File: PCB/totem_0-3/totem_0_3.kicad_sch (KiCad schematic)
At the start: 97 parts, among them J1 MJ-4PP-9, J2 MJ-4PP-9, J3 Conn_01x03_Socket, J4 Conn_01x03_Socket, J5 Conn_01x12_Socket, J6 Conn_01x12_Socket, U1 xiao-ble, U2 xiao-ble, U3 74HC595, U4 74HC595

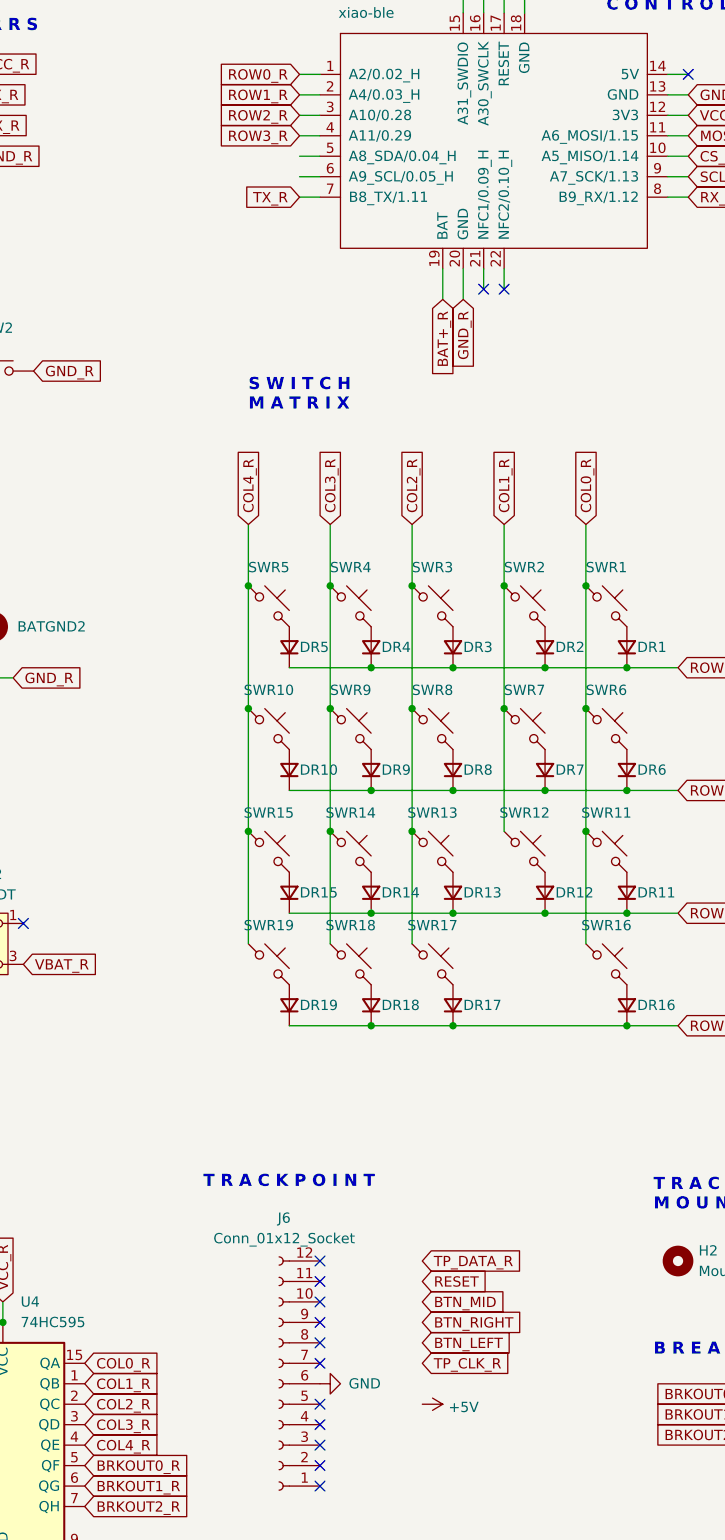
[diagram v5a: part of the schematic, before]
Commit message: sch: wire up trackpoint
Signed-off-by: Anant Thazhemadam <anant.thazhemadam@gmail.com>
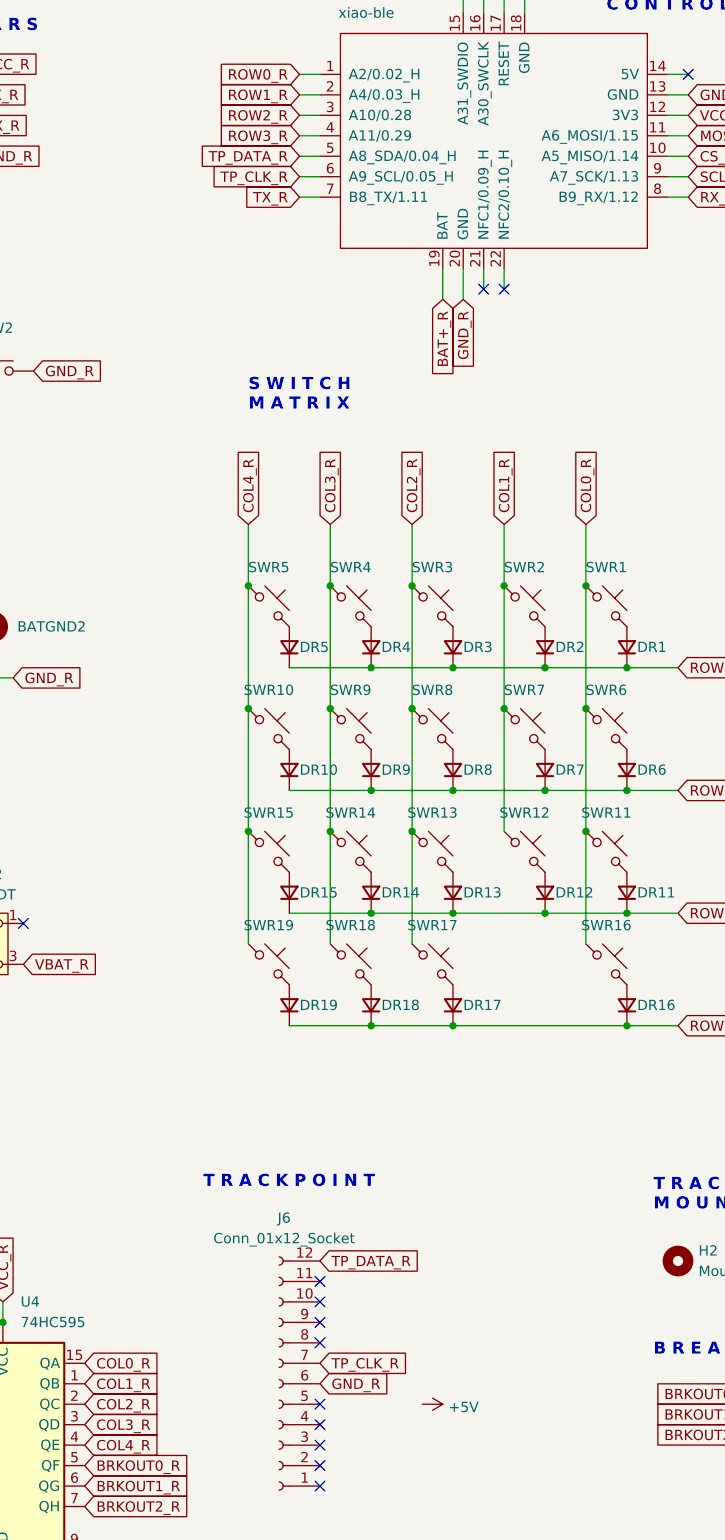
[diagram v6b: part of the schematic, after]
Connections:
- net GND is gone; now on net GND_R: J6.6 (Pin_6)
- net TP_CLK_R: now also J6.7 (Pin_7), U2.6 (A9_SCL/0.05_H)
- net TP_DATA_R: now also J6.12 (Pin_12), U2.5 (A8_SDA/0.04_H)
- no-connect marks 55 -> 53
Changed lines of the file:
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@@
 	)
 	(no_connect
-		(at 257.81 201.93)
-	)
-	(no_connect
 		(at 21.59 207.01)
 	)
@@
 	)
 	(no_connect
-		(at 257.81 189.23)
-	)
-	(no_connect
 		(at 78.74 201.93)
 	)
@@
 		)
 	)
-	(global_label "RESET"
-		(shape input)
-		(at 270.51 191.77 0)
-		(fields_autoplaced yes)
-		(effects
-			(font
-				(size 1.27 1.27)
-			)
-			(justify left)
-		)
-		(property "Intersheetrefs" "${INTERSHEET_REFS}"
-			(at 278.5067 191.77 0)
-			(effects
-				(font
-					(size 1.27 1.27)
-				)
-				(justify left)
-				(hide yes)
-			)
-		)
-	)
 	(global_label "RX_L"
 		(shape input)
@@
 		)
 	)
+	(global_label "TP_DATA_R"
+		(shape input)
+		(at 255.27 52.07 180)
+		(fields_autoplaced yes)
+		(effects
+			(font
+				(size 1.27 1.27)
+			)
+			(justify right)
+		)
+		(property "Intersheetrefs" "${INTERSHEET_REFS}"
+			(at 242.4272 52.07 0)
+			(effects
+				(font
+					(size 1.27 1.27)
+				)
+				(justify right)
+				(hide yes)
+			)
+		)
+	)
 	(global_label "VCC_L"
 		(shape input)
@@
 		)
 	)
-	(global_label "TP_DATA_R"
+	(global_label "GND_R"
 		(shape input)
-		(at 270.51 189.23 0)
+		(at 257.81 204.47 0)
 		(fields_autoplaced yes)
 		(effects
@@
 		)
 		(property "Intersheetrefs" "${INTERSHEET_REFS}"
-			(at 283.3528 189.23 0)
+			(at 266.9033 204.47 0)
 			(effects
 				(font
@@
 		)
 	)
-	(global_label "BTN_RIGHT"
-		(shape input)
-		(at 270.51 196.85 0)
-		(fields_autoplaced yes)
-		(effects
-			(font
-				(size 1.27 1.27)
-			)
-			(justify left)
-		)
-		(property "Intersheetrefs" "${INTERSHEET_REFS}"
-			(at 282.7402 196.85 0)
-			(effects
-				(font
-					(size 1.27 1.27)
-				)
-				(justify left)
-				(hide yes)
-			)
-		)
-	)
 	(global_label "COL3_R"
 		(shape input)
@@
 		)
 	)
+	(global_label "TP_DATA_R"
+		(shape input)
+		(at 257.81 189.23 0)
+		(fields_autoplaced yes)
+		(effects
+			(font
+				(size 1.27 1.27)
+			)
+			(justify left)
+		)
+		(property "Intersheetrefs" "${INTERSHEET_REFS}"
+			(at 270.6528 189.23 0)
+			(effects
+				(font
+					(size 1.27 1.27)
+				)
+				(justify left)
+				(hide yes)
+			)
+		)
+	)
 	(global_label "GND_R"
 		(shape input)
@@
 		)
 	)
-	(global_label "BTN_LEFT"
-		(shape input)
-		(at 270.51 199.39 0)
-		(fields_autoplaced yes)
-		(effects
-			(font
-				(size 1.27 1.27)
-			)
-			(justify left)
-		)
-		(property "Intersheetrefs" "${INTERSHEET_REFS}"
-			(at 281.5306 199.39 0)
-			(effects
-				(font
-					(size 1.27 1.27)
-				)
-				(justify left)
-				(hide yes)
-			)
-		)
-	)
 	(global_label "VBAT_L"
 		(shape input)
@@
 		)
 	)
-	(global_label "TP_CLK_R"
-		(shape input)
-		(at 270.51 201.93 0)
-		(fields_autoplaced yes)
-		(effects
-			(font
-				(size 1.27 1.27)
-			)
-			(justify left)
-		)
-		(property "Intersheetrefs" "${INTERSHEET_REFS}"
-			(at 282.5061 201.93 0)
-			(effects
-				(font
-					(size 1.27 1.27)
-				)
-				(justify left)
-				(hide yes)
-			)
-		)
-	)
 	(global_label "VCC_R"
 		(shape input)
@@
 		)
 	)
+	(global_label "TP_CLK_R"
+		(shape input)
+		(at 257.81 201.93 0)
+		(fields_autoplaced yes)
+		(effects
+			(font
+				(size 1.27 1.27)
+			)
+			(justify left)
+		)
+		(property "Intersheetrefs" "${INTERSHEET_REFS}"
+			(at 269.8061 201.93 0)
+			(effects
+				(font
+					(size 1.27 1.27)
+				)
+				(justify left)
+				(hide yes)
+			)
+		)
+	)
 	(global_label "ROW2_R"
 		(shape input)
@@
 		)
 	)
-	(global_label "BTN_MID"
+	(global_label "TP_CLK_R"
 		(shape input)
-		(at 270.51 194.31 0)
+		(at 255.27 54.61 180)
 		(fields_autoplaced yes)
 		(effects
@@
 				(size 1.27 1.27)
 			)
-			(justify left)
+			(justify right)
 		)
 		(property "Intersheetrefs" "${INTERSHEET_REFS}"
-			(at 280.6235 194.31 0)
+			(at 243.2739 54.61 0)
 			(effects
 				(font
 					(size 1.27 1.27)
 				)
-				(justify left)
+				(justify right)
 				(hide yes)
 			)
@@
 					(unit 1)
 				)
-			)
-		)
-	)
-	(symbol
-		(lib_id "power:GND")
-		(at 257.81 204.47 90)
-		(unit 1)
-		(exclude_from_sim no)
-		(in_bom yes)
-		(on_board yes)
-		(dnp no)
-		(fields_autoplaced yes)
-		(property "Reference" "#PWR01"
-			(at 264.16 204.47 0)
-			(effects
-				(font
-					(size 1.27 1.27)
-				)
-				(hide yes)
-			)
-		)
-		(property "Value" "GND"
-			(at 261.366 204.47 90)
-			(effects
-				(font
-					(size 1.27 1.27)
-				)
-				(justify right)
-			)
-		)
-		(property "Footprint" ""
-			(at 257.81 204.47 0)
-			(effects
-				(font
-					(size 1.27 1.27)
-				)
-				(hide yes)
-			)
-		)
-		(property "Datasheet" ""
-			(at 257.81 204.47 0)
-			(effects
-				(font
-					(size 1.27 1.27)
-				)
-				(hide yes)
-			)
-		)
-		(property "Description" "Power symbol creates a global label with name \"GND\" , ground"
-			(at 257.81 204.47 0)
-			(effects
-				(font
-					(size 1.27 1.27)
-				)
-				(hide yes)
-			)
-		)
-		(pin "1"
-		)
-		(instances
-			(project "totem_0_3"
-				(path "/4d1e609f-5432-4afb-8ee7-7d2d9aaaee48"
-					(reference "#PWR01")
-					(unit 1)
-				)

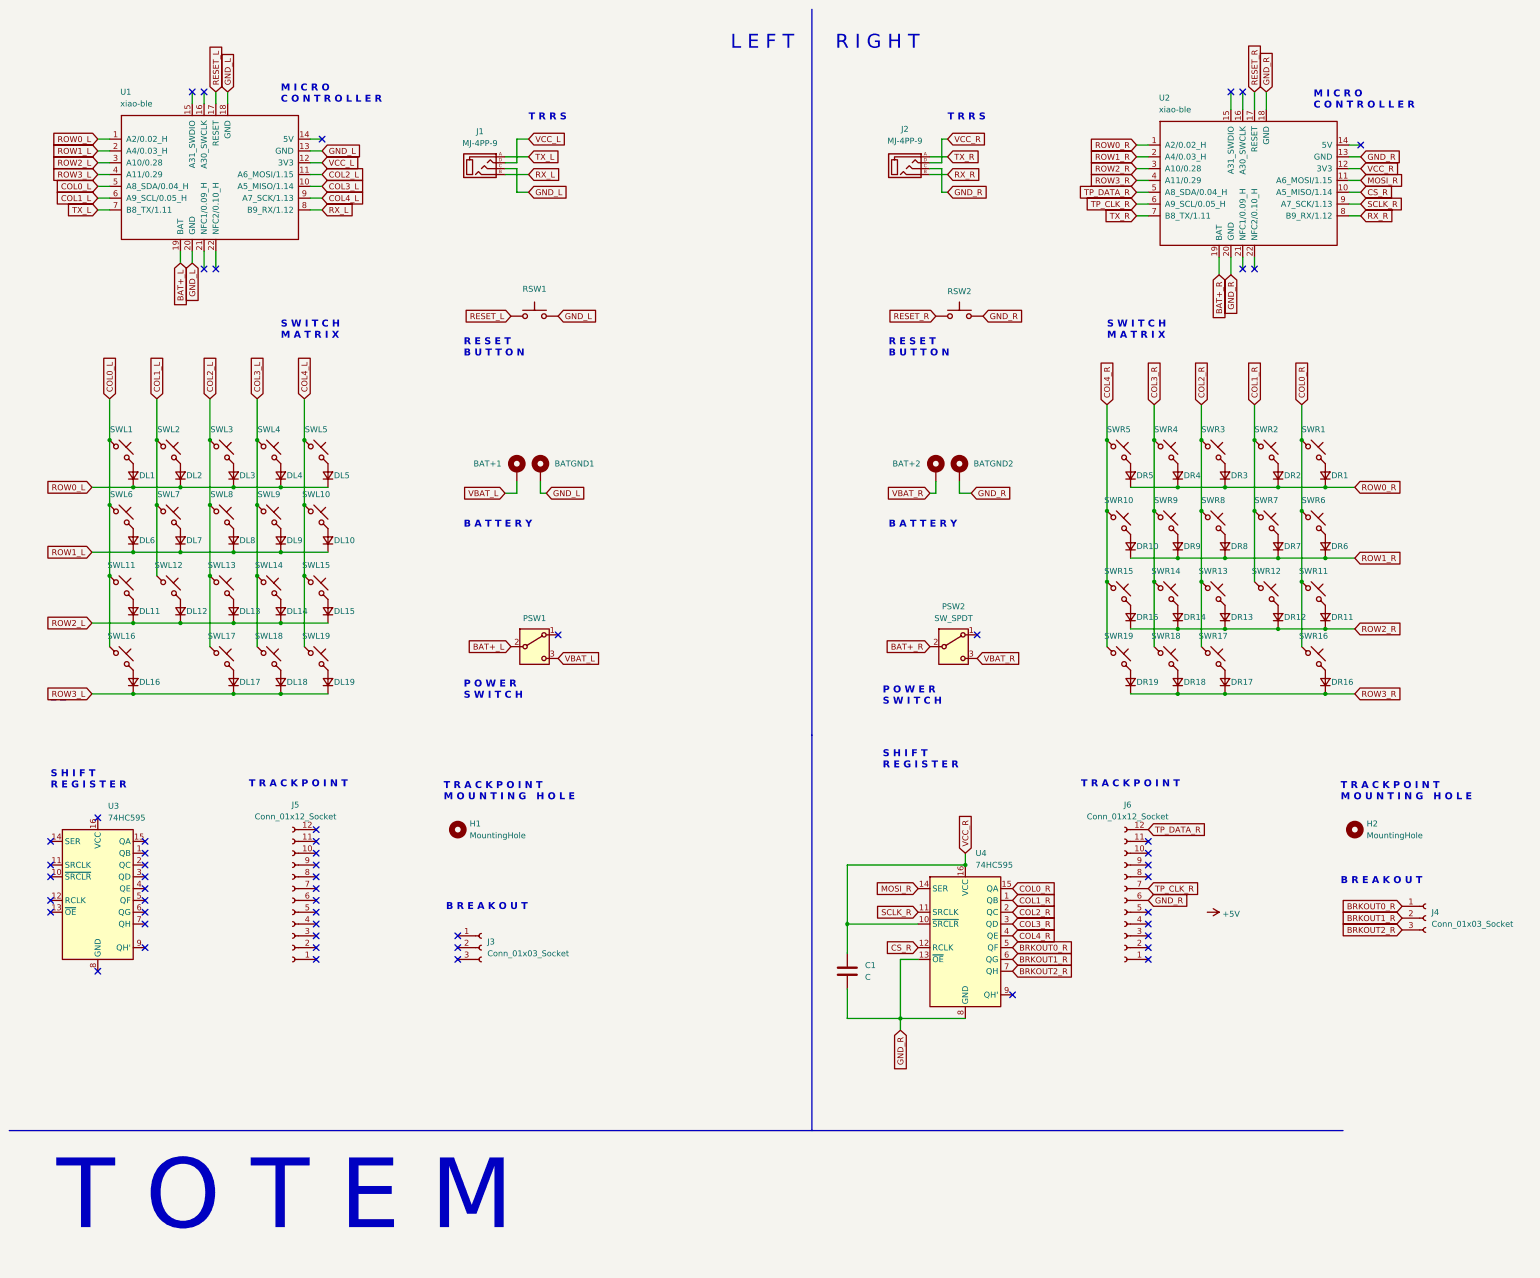
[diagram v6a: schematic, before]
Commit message: pcb: remove lhs trackpoint
Signed-off-by: Anant Thazhemadam <anant.thazhemadam@gmail.com>
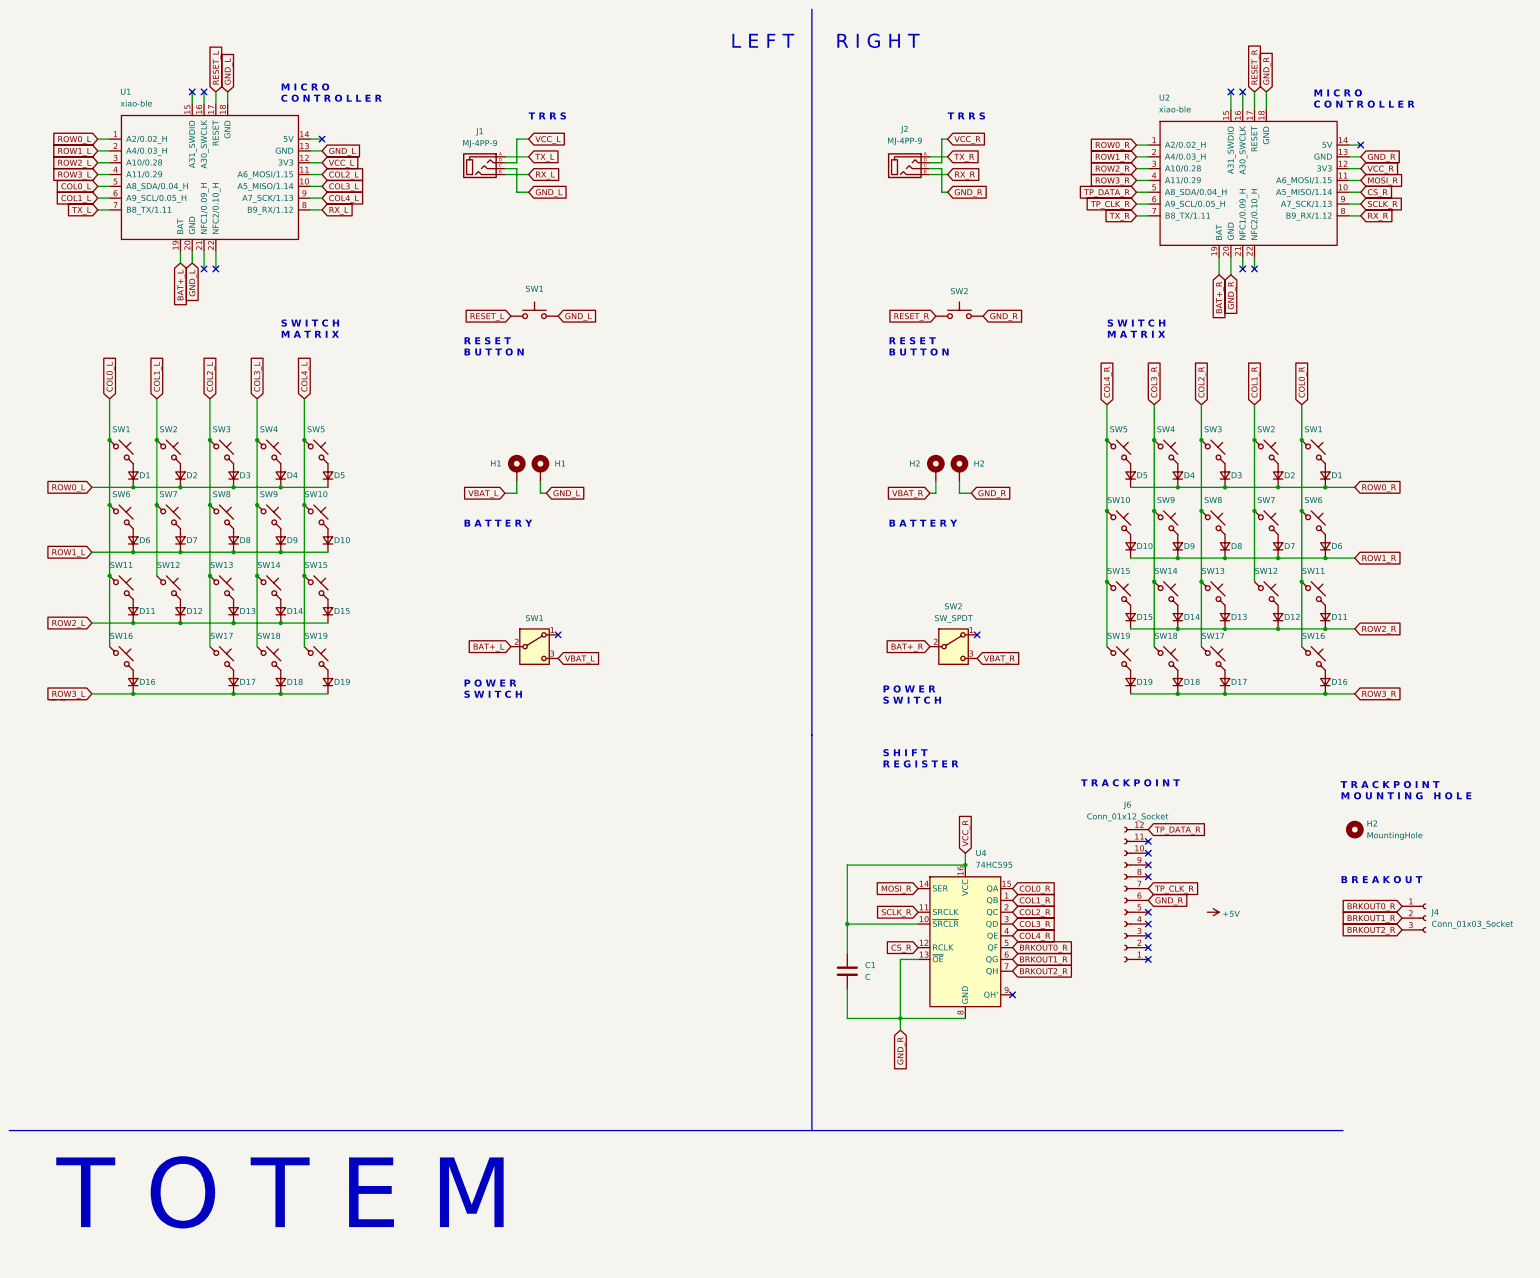
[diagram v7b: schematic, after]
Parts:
- removed H1: MountingHole, TOTEMlib:TPSensorModule, symbol Mechanical:MountingHole
- removed J3: Conn_01x03_Socket, Connector_PinHeader_2.54mm:PinHeader_1x03_P2.54mm_Vertical, symbol Connector:Conn_01x03_Socket
- removed J5: Conn_01x12_Socket, Connector_FFC-FPC:TE_1-84953-2_1x12-1MP_P1.0mm_Horizontal, symbol Connector:Conn_01x12_Socket
- removed U3: 74HC595, Package_SO:SOIC-16_3.9x9.9mm_P1.27mm, symbol 74xx:74HC595
- renumbered DL1 to D1, DR1 to D1, DL10 to D10, DR10 to D10, DR11 to D11, DL11 to D11, DR12 to D12, DL12 to D12, DR13 to D13, DL13 to D13, DR14 to D14, DL14 to D14, DR15 to D15, DL15 to D15, DR16 to D16, DL16 to D16, DR17 to D17, DL17 to D17, DL18 to D18, DR18 to D18, DL19 to D19, DR19 to D19, DL2 to D2, DR2 to D2, DL3 to D3, DR3 to D3, DR4 to D4, DL4 to D4, DR5 to D5, DL5 to D5, DR6 to D6, DL6 to D6, DL7 to D7, DR7 to D7, DL8 to D8, DR8 to D8, DR9 to D9, DL9 to D9, BAT+1 to H1, BATGND1 to H1, BATGND2 to H2, BAT+2 to H2, PSW1 to SW1, RSW1 to SW1, SWL1 to SW1, SWR1 to SW1, SWR10 to SW10, SWL10 to SW10, SWL11 to SW11, SWR11 to SW11, SWR12 to SW12, SWL12 to SW12, SWR13 to SW13, SWL13 to SW13, SWL14 to SW14, SWR14 to SW14, SWL15 to SW15, SWR15 to SW15, SWL16 to SW16, SWR16 to SW16, SWL17 to SW17, SWR17 to SW17, SWL18 to SW18, SWR18 to SW18, SWL19 to SW19, SWR19 to SW19, SWR2 to SW2, PSW2 to SW2, SWL2 to SW2, RSW2 to SW2, SWR3 to SW3, SWL3 to SW3, SWL4 to SW4, SWR4 to SW4, SWR5 to SW5, SWL5 to SW5, SWR6 to SW6, SWL6 to SW6, SWL7 to SW7, SWR7 to SW7, SWR8 to SW8, SWL8 to SW8, SWL9 to SW9, SWR9 to SW9
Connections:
- no-connect marks 53 -> 22

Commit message: pcb: fix drc errors
Signed-off-by: Anant Thazhemadam <anant.thazhemadam@gmail.com>
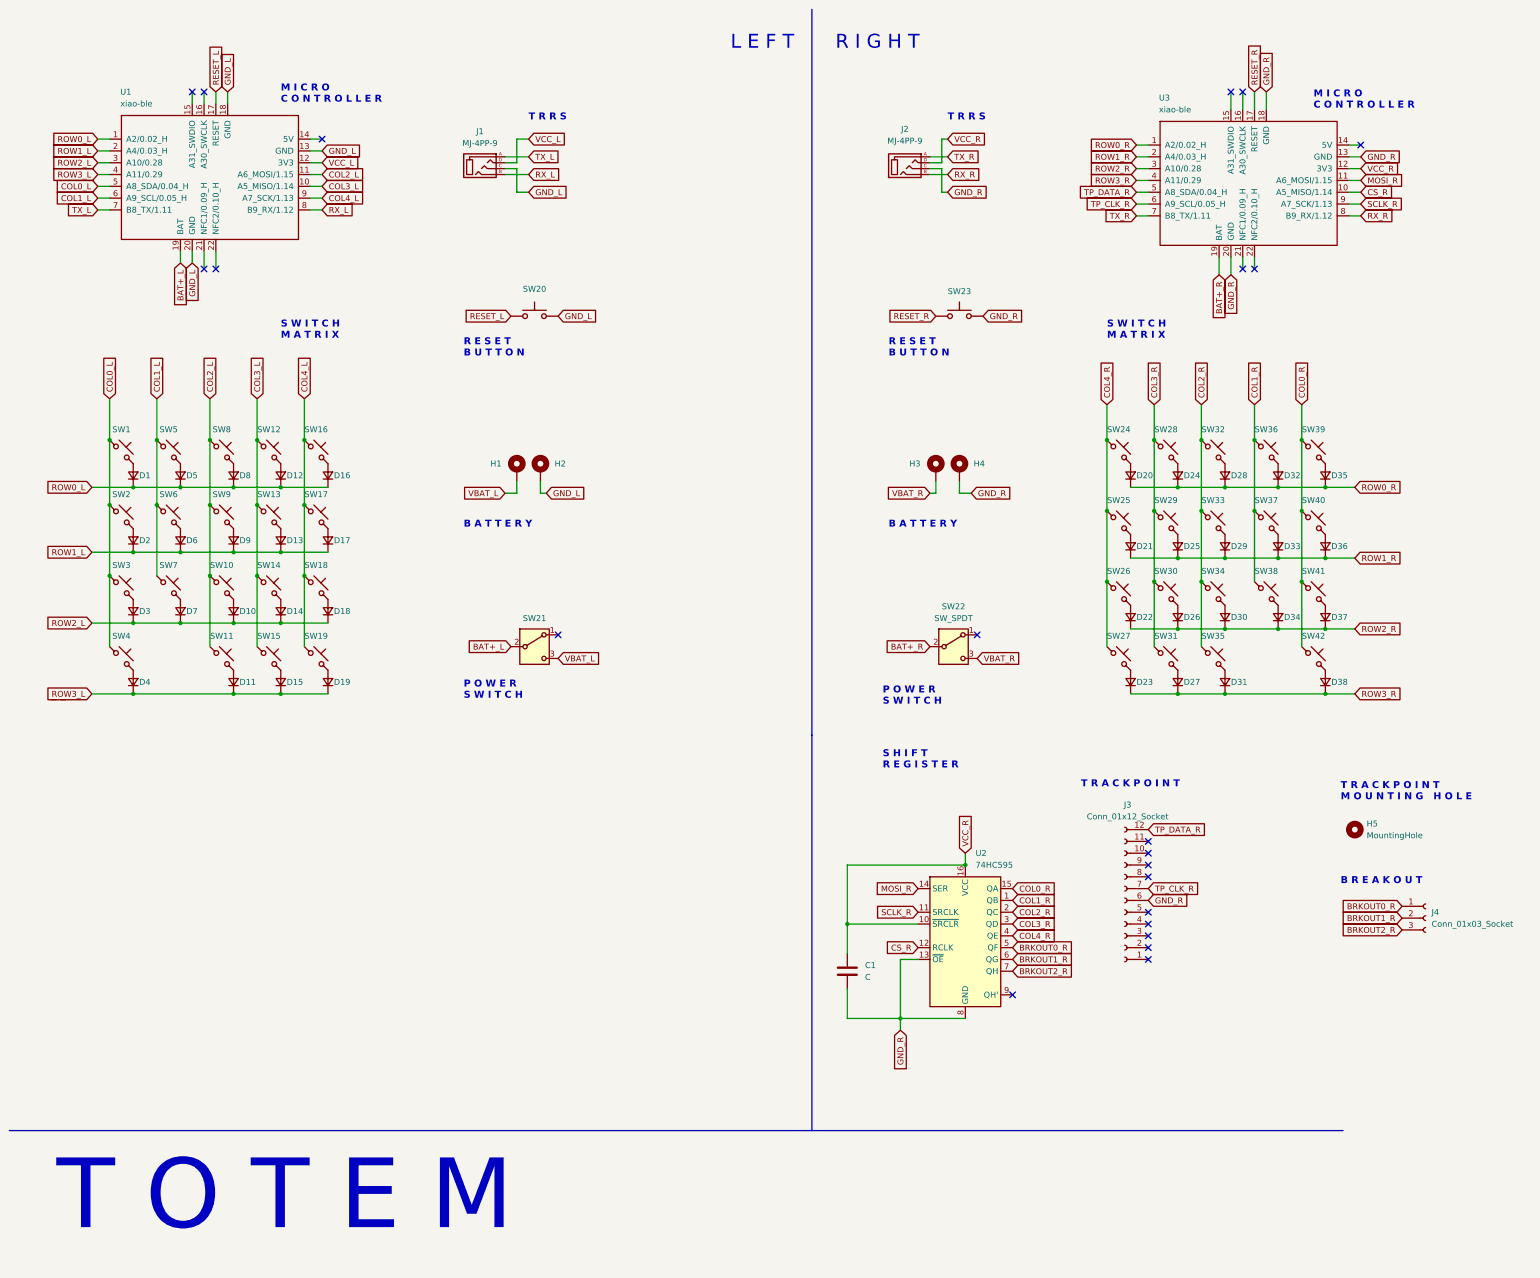
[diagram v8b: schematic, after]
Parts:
- renumbered D13 to D10, D17 to D11, D4 to D12, D9 to D13, D18 to D15, D5 to D16, D10 to D17, D15 to D18, D6 to D2, D5 to D20, D10 to D21, D15 to D22, D19 to D23, D4 to D24, D9 to D25, D14 to D26, D18 to D27, D3 to D28, D8 to D29, D11 to D3, D13 to D30, D17 to D31, D2 to D32, D7 to D33, D12 to D34, D1 to D35, D6 to D36, D11 to D37, D16 to D38, D16 to D4, D2 to D5, D7 to D6, D12 to D7, D3 to D8, D8 to D9, H1 to H2, H2 to H3, H2 to H4, H2 to H5, J6 to J3, SW13 to SW10, SW17 to SW11, SW4 to SW12, SW9 to SW13, SW18 to SW15, SW5 to SW16, SW10 to SW17, SW15 to SW18, SW6 to SW2, SW1 to SW20, SW1 to SW21, SW2 to SW22, SW2 to SW23, SW5 to SW24, SW10 to SW25, SW15 to SW26, SW19 to SW27, SW4 to SW28, SW9 to SW29, SW11 to SW3, SW14 to SW30, SW18 to SW31, SW3 to SW32, SW8 to SW33, SW13 to SW34, SW17 to SW35, SW2 to SW36, SW7 to SW37, SW12 to SW38, SW1 to SW39, SW16 to SW4, SW6 to SW40, SW11 to SW41, SW16 to SW42, SW2 to SW5, SW7 to SW6, SW12 to SW7, SW3 to SW8, SW8 to SW9, U4 to U2, U2 to U3
